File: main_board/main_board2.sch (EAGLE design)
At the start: 18 parts, among them J1 Bar30, J2 Temp/Hum, J3 LED

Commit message: connected some wires just to test github and to see if gitignore is working.
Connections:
- net N$14: now also J3.4
- net N$15: now also J3.3
- net N$16: now also J3.2
- net N$17: now also J3.1
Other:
- moved on the sheet: J3
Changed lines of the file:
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@@
 <instance part="P+2" gate="1" x="-55.88" y="154.94"/>
 <instance part="GND4" gate="1" x="-55.88" y="139.7"/>
-<instance part="J3" gate="G$1" x="-104.14" y="58.42"/>
+<instance part="J3" gate="G$1" x="-68.58" y="71.12"/>
 </instances>
 <busses>
@@
 <pinref part="LEDROPE" gate="A" pin="4"/>
 <wire x1="129.54" y1="109.22" x2="129.54" y2="96.52" width="0.1524" layer="91"/>
-<wire x1="-63.5" y1="96.52" x2="-63.5" y2="81.28" width="0.1524" layer="91"/>
+<wire x1="-63.5" y1="96.52" x2="-63.5" y2="76.2" width="0.1524" layer="91"/>
 <wire x1="129.54" y1="96.52" x2="-63.5" y2="96.52" width="0.1524" layer="91"/>
+<pinref part="J3" gate="G$1" pin="4"/>
 </segment>
 </net>
@@
 <wire x1="132.08" y1="106.68" x2="132.08" y2="93.98" width="0.1524" layer="91"/>
 <wire x1="132.08" y1="93.98" x2="-60.96" y2="93.98" width="0.1524" layer="91"/>
-<wire x1="-60.96" y1="93.98" x2="-60.96" y2="81.28" width="0.1524" layer="91"/>
+<wire x1="-60.96" y1="93.98" x2="-60.96" y2="73.66" width="0.1524" layer="91"/>
 <pinref part="LEDROPE" gate="A" pin="2"/>
+<pinref part="J3" gate="G$1" pin="3"/>
+<wire x1="-60.96" y1="73.66" x2="-63.5" y2="73.66" width="0.1524" layer="91"/>
 </segment>
 </net>
@@
 <wire x1="139.7" y1="86.36" x2="139.7" y2="91.44" width="0.1524" layer="91"/>
 <wire x1="139.7" y1="91.44" x2="-58.42" y2="91.44" width="0.1524" layer="91"/>
-<wire x1="-58.42" y1="91.44" x2="-58.42" y2="83.82" width="0.1524" layer="91"/>
 <pinref part="LEDROPE" gate="A" pin="1"/>
+<wire x1="-58.42" y1="91.44" x2="-58.42" y2="71.12" width="0.1524" layer="91"/>
+<pinref part="J3" gate="G$1" pin="2"/>
+<wire x1="-58.42" y1="71.12" x2="-63.5" y2="71.12" width="0.1524" layer="91"/>
 </segment>
 </net>
@@
 <wire x1="137.16" y1="83.82" x2="137.16" y2="88.9" width="0.1524" layer="91"/>
 <wire x1="137.16" y1="88.9" x2="-55.88" y2="88.9" width="0.1524" layer="91"/>
-<wire x1="-55.88" y1="88.9" x2="-55.88" y2="83.82" width="0.1524" layer="91"/>
 <pinref part="LEDROPE" gate="A" pin="3"/>
+<wire x1="-55.88" y1="88.9" x2="-55.88" y2="68.58" width="0.1524" layer="91"/>
+<pinref part="J3" gate="G$1" pin="1"/>
+<wire x1="-55.88" y1="68.58" x2="-63.5" y2="68.58" width="0.1524" layer="91"/>
 </segment>
 </net>

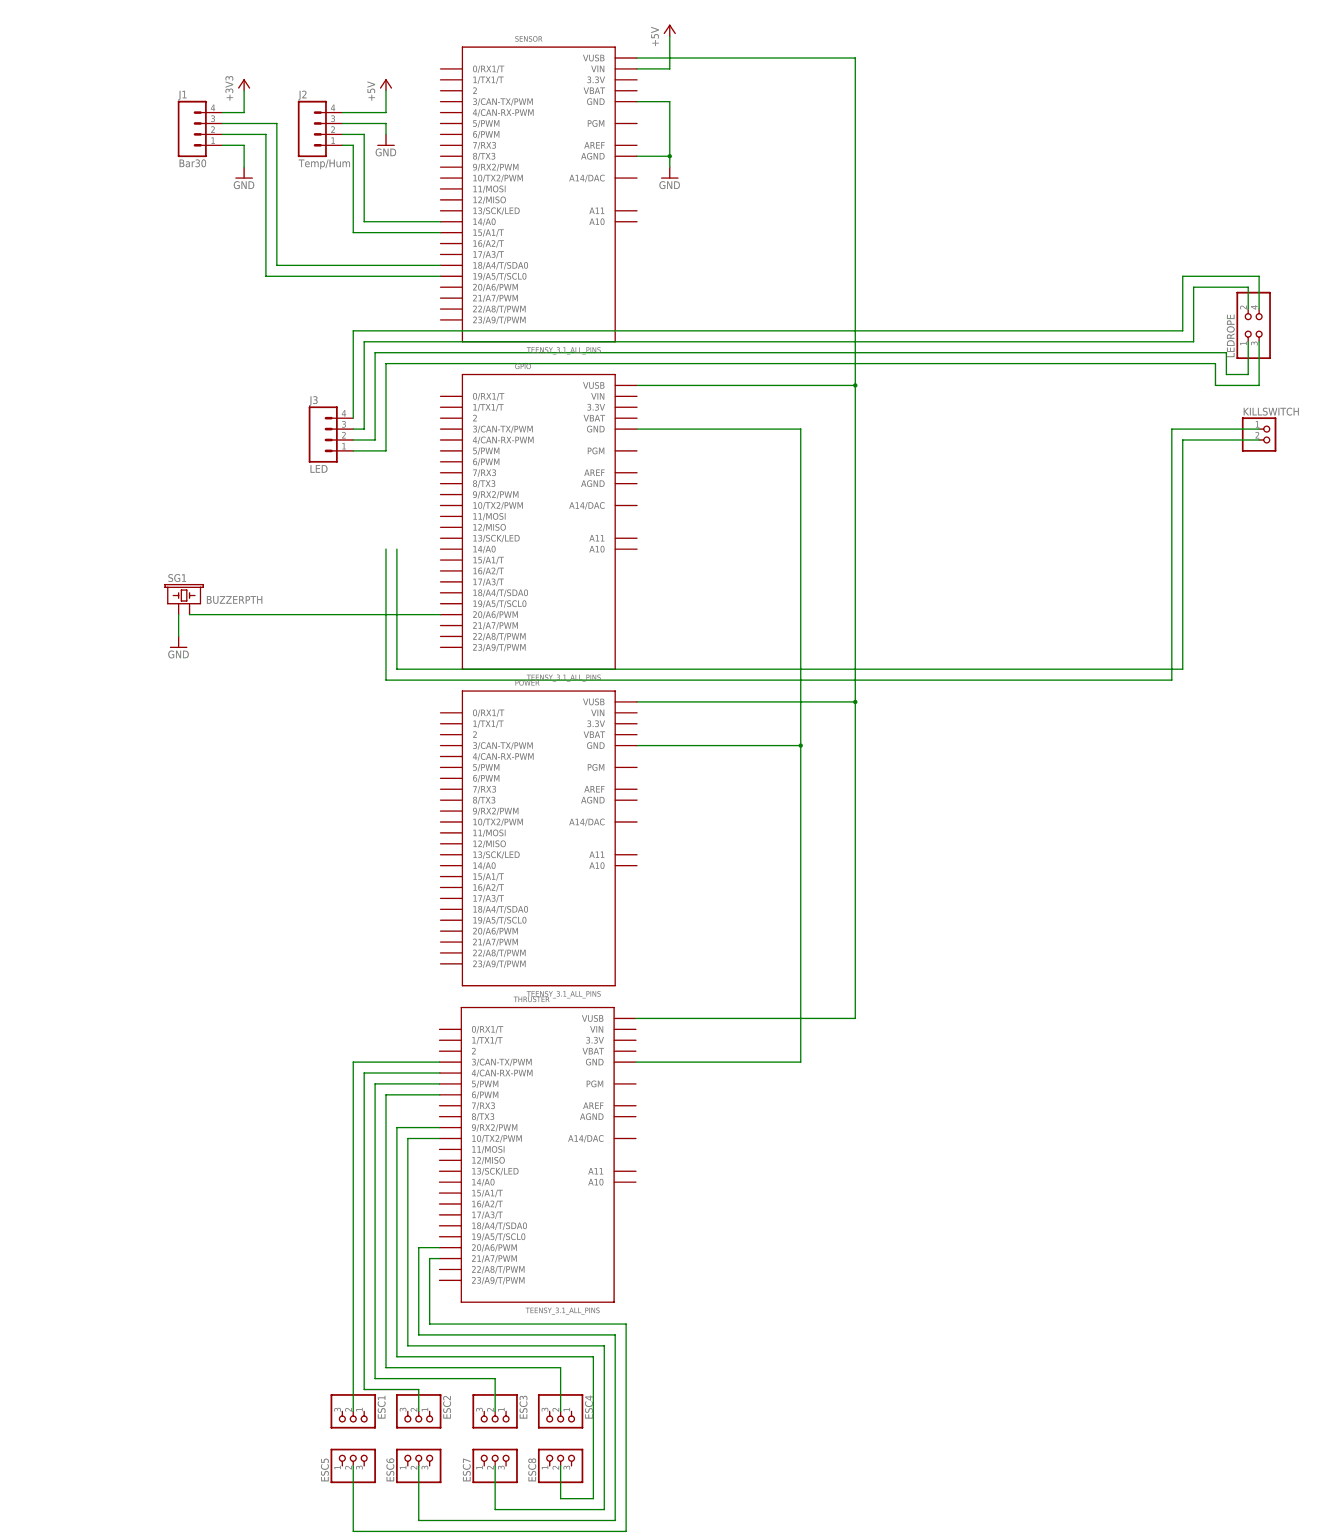
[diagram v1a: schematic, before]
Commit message: added necessary components to drive LEDs
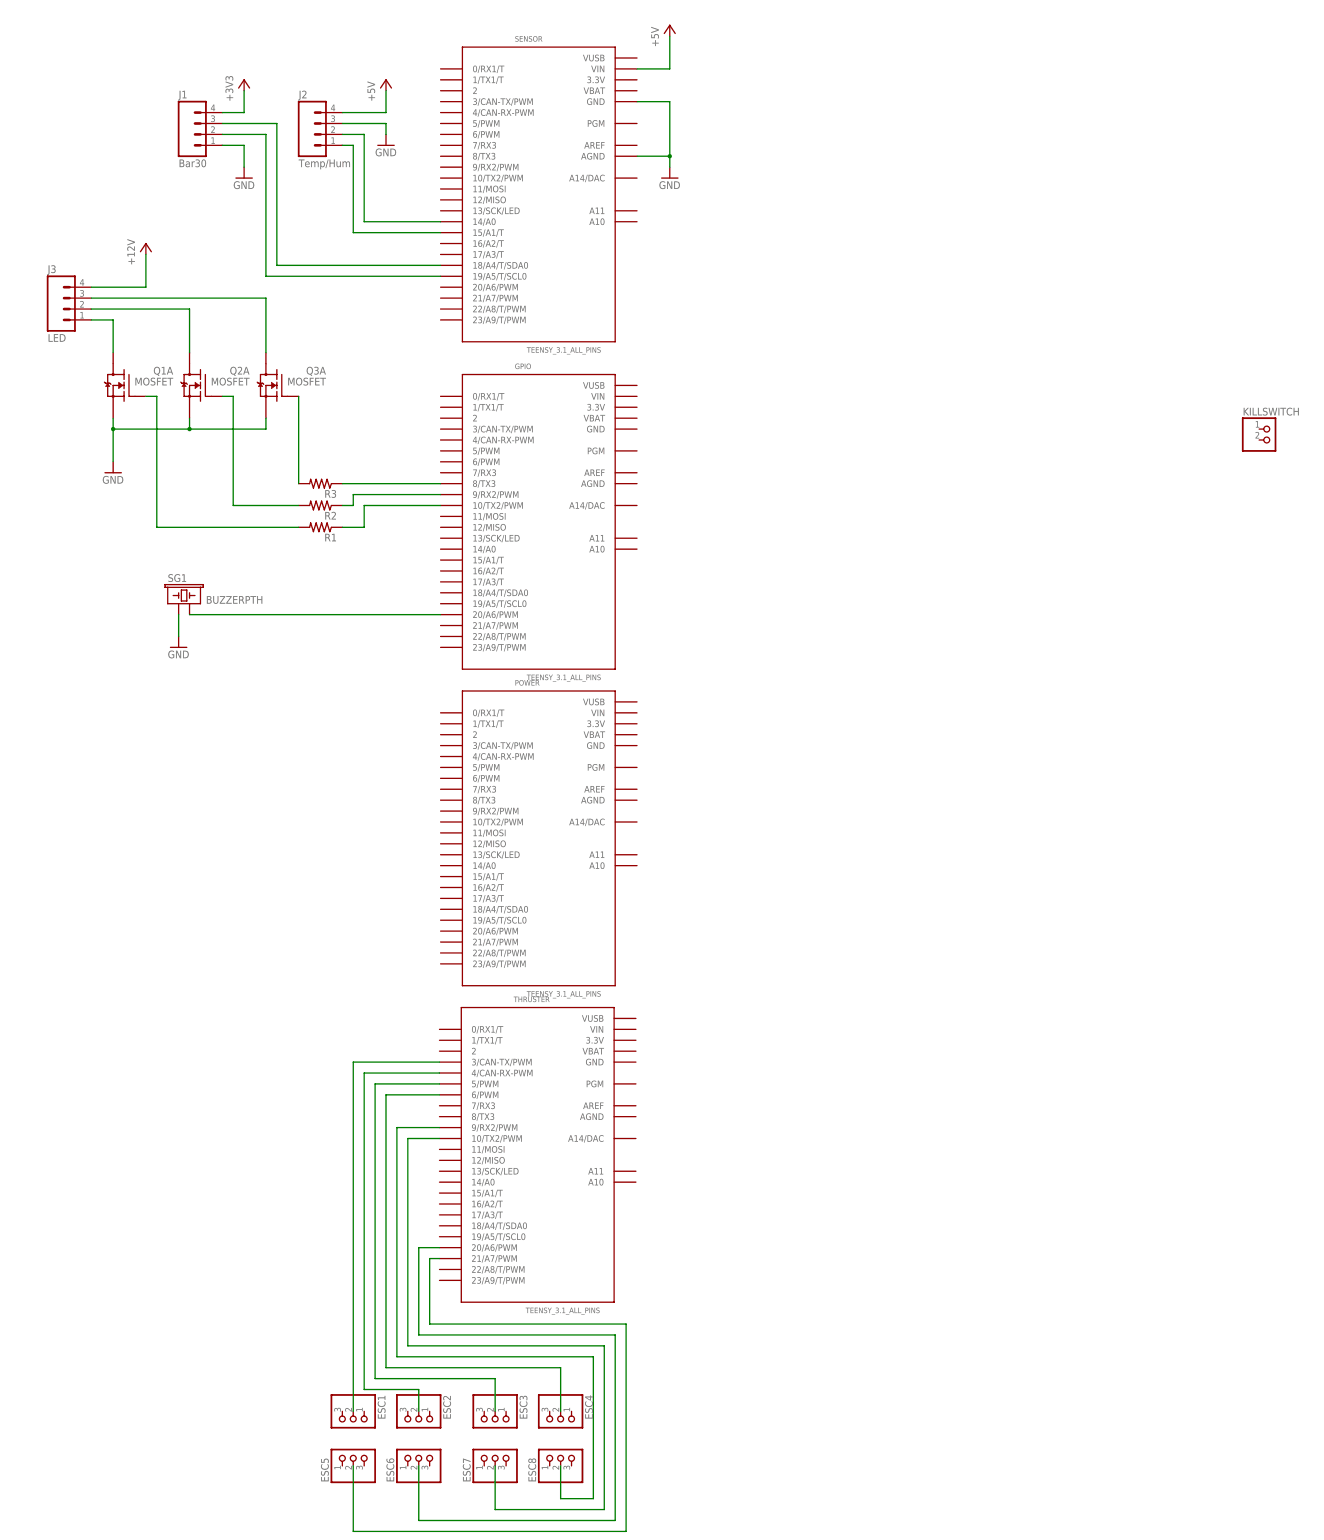
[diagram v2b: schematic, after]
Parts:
- removed LEDROPE: (no value), pinhead:PINHD-2X2
- added Q1, Q2, Q3: MOSFET, SparkFun-DiscreteSemi:MOSFET-NCHANNEL_DUALFDMA1024NZ
- added R1, R2, R3: (no value), SparkFun-Resistors:RESISTORPTH-1/4W
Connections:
- removed net N$20: GPIO.VUSB, POWER.VUSB, SENSOR.VUSB, THRUSTER.VUSB
- new net +12V: J3.4
- new net N$23: J3.1, Q1A.D1
- new net N$24: J3.2, Q2A.D1
- net GND: now also Q1A.S, Q2A.S, Q3A.S
- net N$12: now also GPIO.8/TX3, R3.1; no longer GPIO.GND, POWER.GND, THRUSTER.GND
- net N$14: now also GPIO.9/RX2/PWM, R2.1; no longer J3.4, LEDROPE.4
- net N$15: now also GPIO.10/TX2/PWM, R1.1; no longer J3.3, LEDROPE.2
- net N$16: now also Q3A.G, R3.2; no longer J3.2, LEDROPE.1
- net N$17: now also Q2A.G, R2.2; no longer J3.1, LEDROPE.3
- net N$18: now also Q1A.G, R1.2; no longer KILLSWITCH.1
- net N$19: now also J3.3, Q3A.D1; no longer KILLSWITCH.2
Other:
- moved on the sheet: J3

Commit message: updated thruster headers. can't decide between using sparkfun header library or default.
the sparkfun one doesn't have dual-row pin headers.
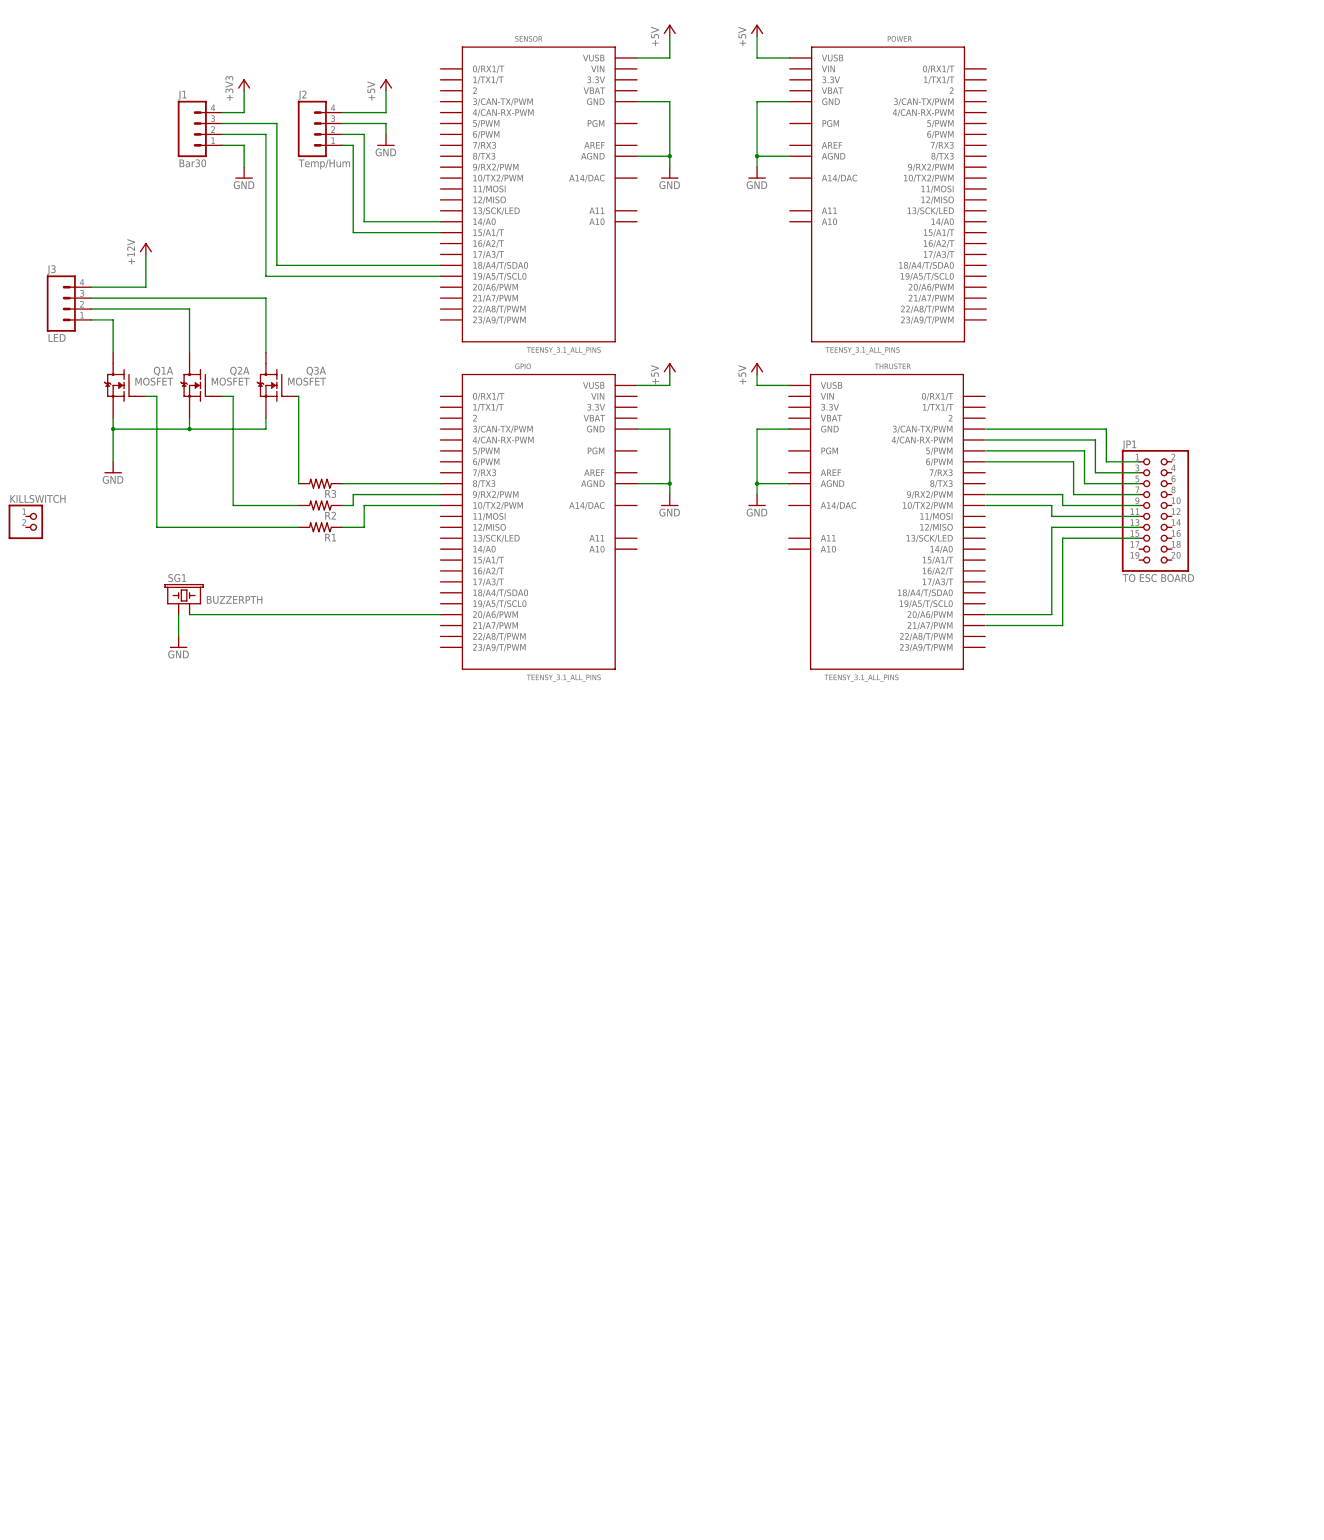
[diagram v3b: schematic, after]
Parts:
- removed ESC1, ESC2, ESC3, ESC4, ESC5, ESC6, ESC7, ESC8: (no value), pinhead:PINHD-1X3
- added JP1: TO ESC BOARD, pinhead:PINHD-2X10
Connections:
- net +5V: now also GPIO.VUSB, POWER.VUSB, SENSOR.VUSB; no longer SENSOR.VIN
- net GND: now also GPIO.AGND, GPIO.GND, POWER.AGND, POWER.GND
- net N$2: now also JP1.1; no longer ESC1.2, THRUSTER.3/CAN-TX/PWM
- net N$3: now also JP1.3; no longer ESC2.2, THRUSTER.4/CAN-RX-PWM
- net N$4: now also JP1.5; no longer ESC3.2, THRUSTER.5/PWM
- net N$5: now also JP1.7; no longer ESC4.2, THRUSTER.6/PWM
- net N$6: now also JP1.9; no longer ESC8.2, THRUSTER.9/RX2/PWM
- net N$7: now also JP1.11; no longer ESC7.2, THRUSTER.10/TX2/PWM
- net N$8: now also JP1.13; no longer ESC6.2, THRUSTER.20/A6/PWM
- net N$9: now also JP1.15; no longer THRUSTER.21/A7/PWM
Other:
- moved on the sheet: KILLSWITCH, POWER, THRUSTER
